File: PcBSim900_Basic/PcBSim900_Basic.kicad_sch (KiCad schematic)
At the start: 28 parts, among them J11 ANT, J14 SIM_Card, J5 Conn_02x03_Odd_Even, Q3 BC817, Q4 BC817, Q5 BC817, U8 SIM900

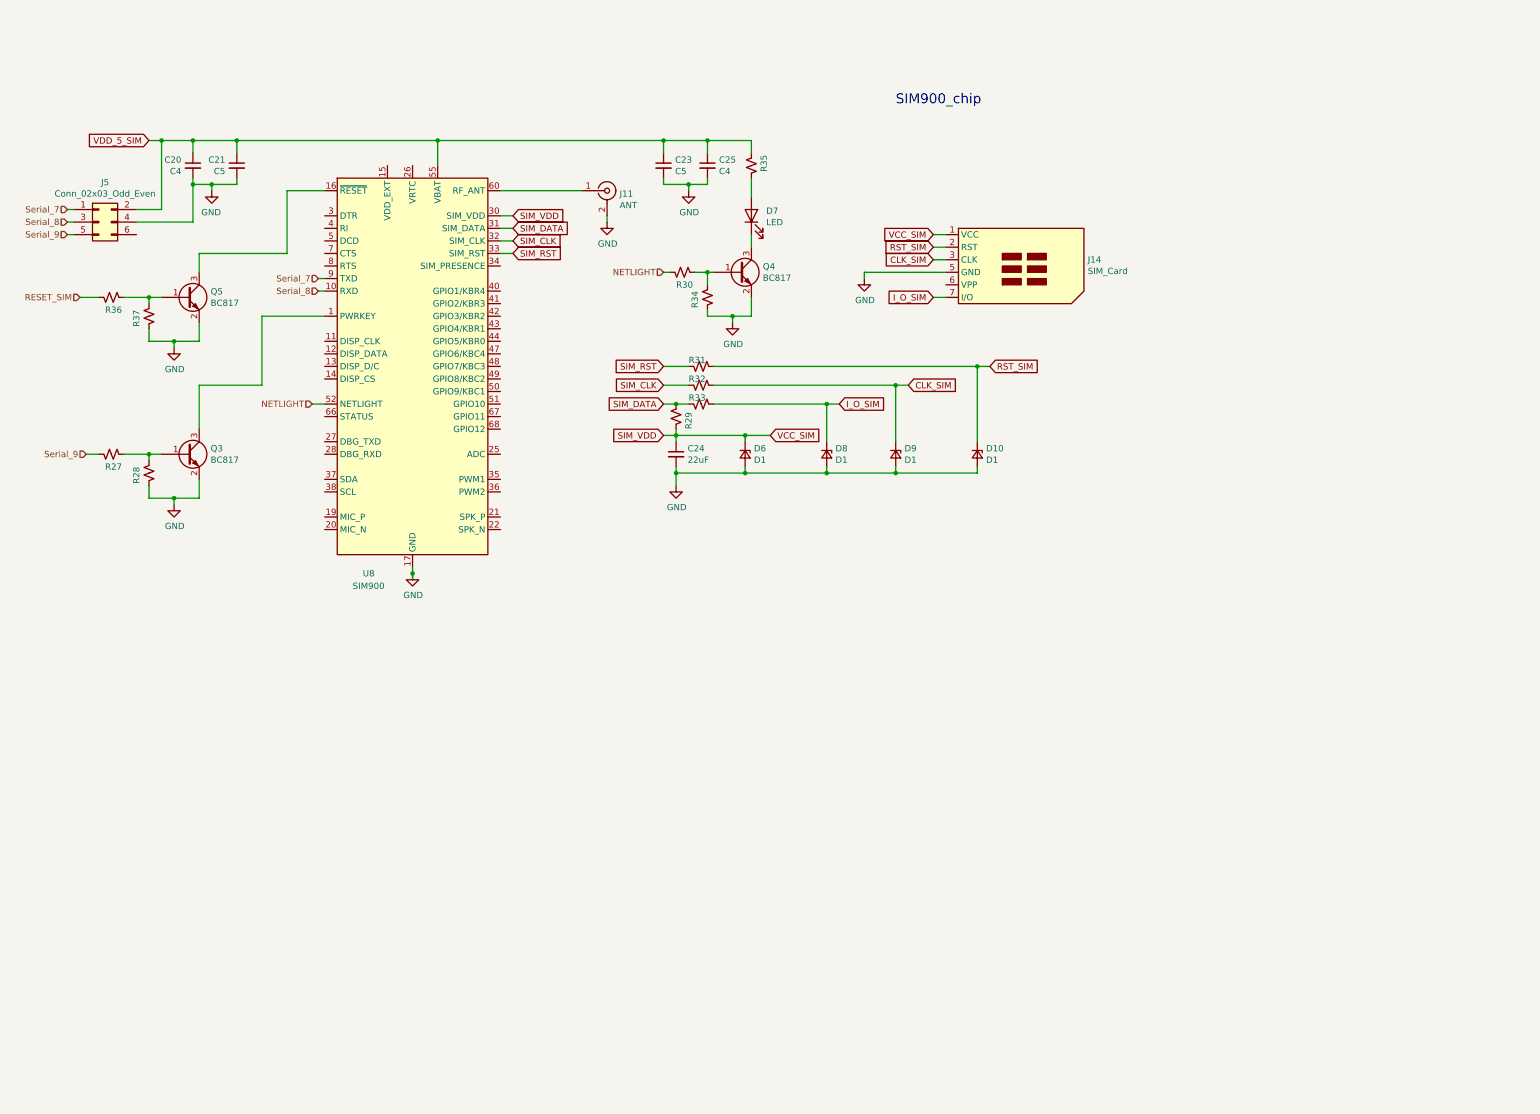
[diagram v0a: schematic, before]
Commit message: add atmega2560
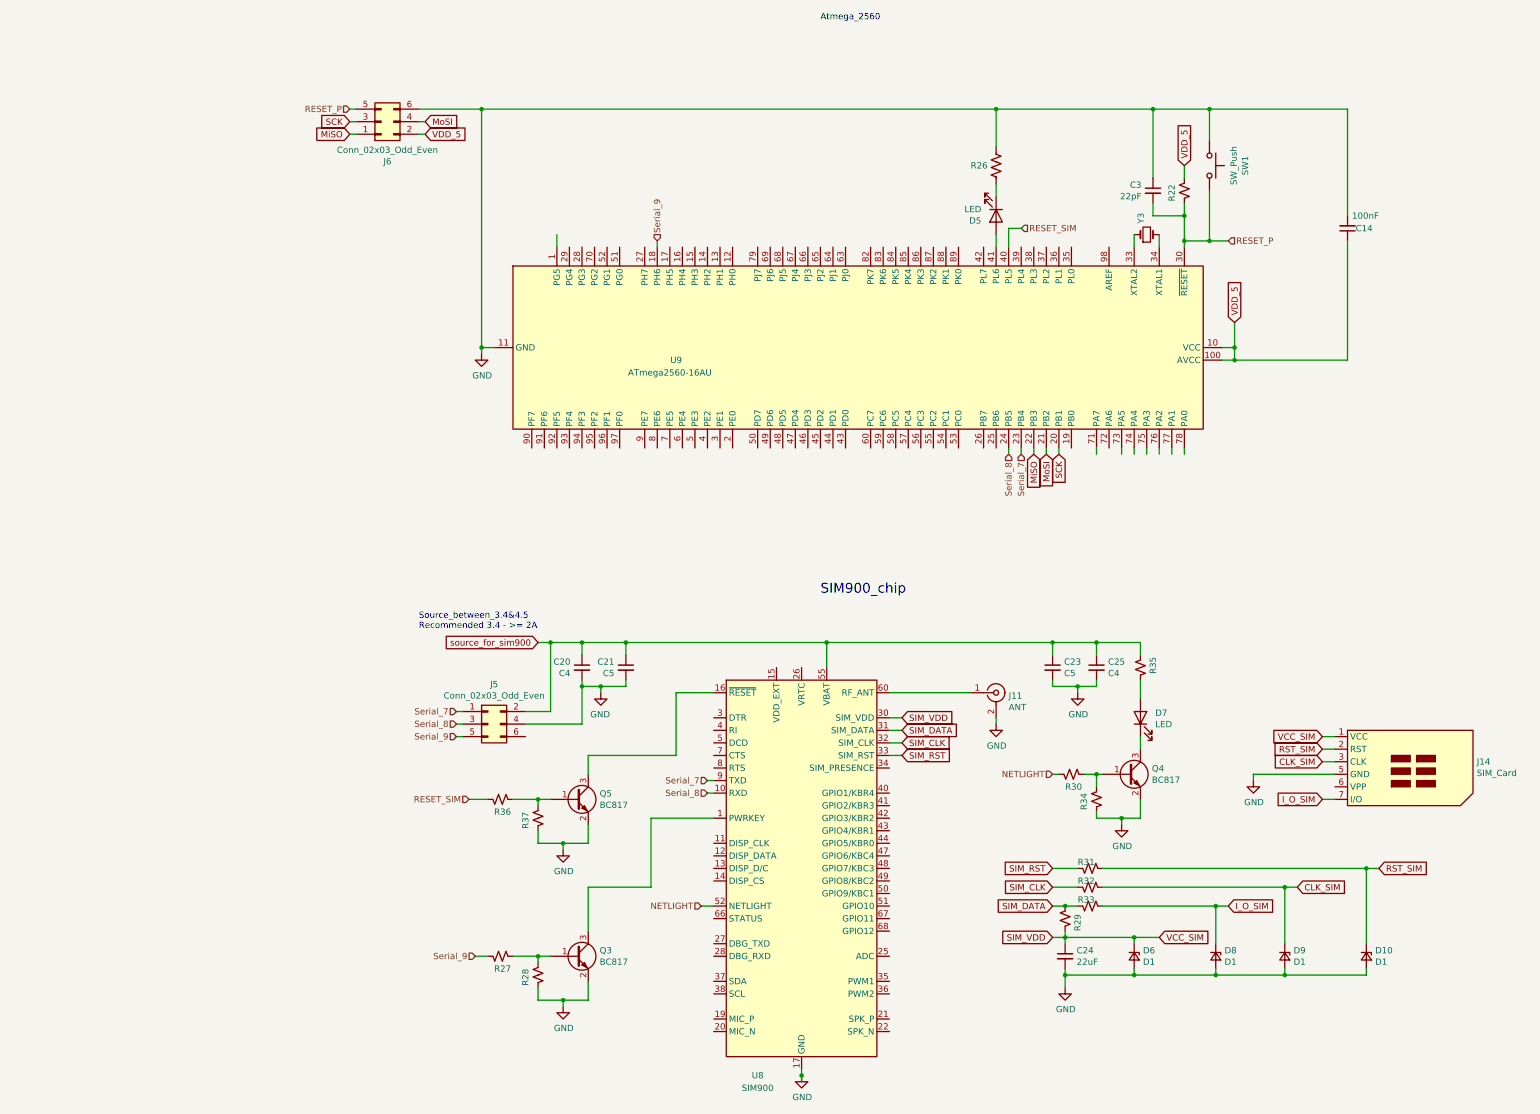
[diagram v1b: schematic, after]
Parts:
- added C14: 100nF, Capacitor_THT:C_Disc_D7.5mm_W2.5mm_P5.00mm, symbol Device:C_Small
- added C3: 22pF, Capacitor_THT:C_Disc_D7.5mm_W2.5mm_P5.00mm, symbol Device:C_Small
- added D5: LED, LED_THT:LED_D3.0mm_Clear, symbol Device:LED
- added J6: Conn_02x03_Odd_Even, Connector_PinSocket_2.54mm:PinSocket_2x03_P2.54mm_Vertical, symbol Connector_Generic:Conn_02x03_Odd_Even
- added R22: R_Small_US, Resistor_THT:R_Axial_DIN0204_L3.6mm_D1.6mm_P5.08mm_Horizontal, symbol Device:R_Small_US
- added R26: R_US, Resistor_THT:R_Axial_DIN0204_L3.6mm_D1.6mm_P1.90mm_Vertical, symbol Device:R_US
- added SW1: SW_Push, Button_Switch_THT:SW_PUSH_6mm_H4.3mm, symbol Switch:SW_Push
- added U9: ATmega2560-16AU, Package_QFP:TQFP-100_14x14mm_P0.5mm, symbol DISEÑO_PCB-rescue:ATmega2560-16AU-MCU_Microchip_ATmega
- added Y3: Crystal_Small, Crystal:Crystal_HC52-6mm_Vertical, symbol Device:Crystal_Small
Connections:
- net GND: now also C14.2, C3.1, J6.6 (Pin_6), R26.2, SW1.1, U9.11 (GND), U9.32 (GND), U9.62 (GND), U9.81 (GND), U9.99 (GND)
- net RESET_SIM: now also U9.40 (PL5)
- net Serial_7: now also U9.23 (PB4)
- net Serial_8: now also U9.24 (PB5)
- net Serial_9: now also U9.18 (PH6)
- net VDD_5_SIM renamed source_for_sim900
- new net: U9.33 (XTAL2), Y3.1
- new net: U9.34 (XTAL1), Y3.2
- new net: D5.2 (A), U9.41 (PL6)
- new net: D5.1 (K), R26.1
- new net MiSO: J6.1 (Pin_1), U9.22 (PB3)
- new net MoSI: J6.4 (Pin_4), U9.21 (PB2)
- new net RESET_P: C3.2, J6.5 (Pin_5), R22.1, SW1.2, U9.30 (~{RESET})
- new net SCK: J6.3 (Pin_3), U9.20 (PB1)
- new net VDD_5: C14.1, J6.2 (Pin_2), R22.2, U9.10 (VCC), U9.100 (AVCC), U9.31 (VCC), U9.61 (VCC), U9.80 (VCC)
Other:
- note added: "Atmega_2560"
- note added: "Source_between_3.4&4.5 Recommended 3.4 - >= 2A"
